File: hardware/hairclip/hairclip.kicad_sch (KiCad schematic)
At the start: 18 parts, among them J1 Conn_Coaxial_Small, J2 Conn_ARM_SWD_TagConnect_TC2030, U1 NRF52840-CKAA-R, U2 MIC5365-3.3YD5, X1 32MHz, X2 32kHz768

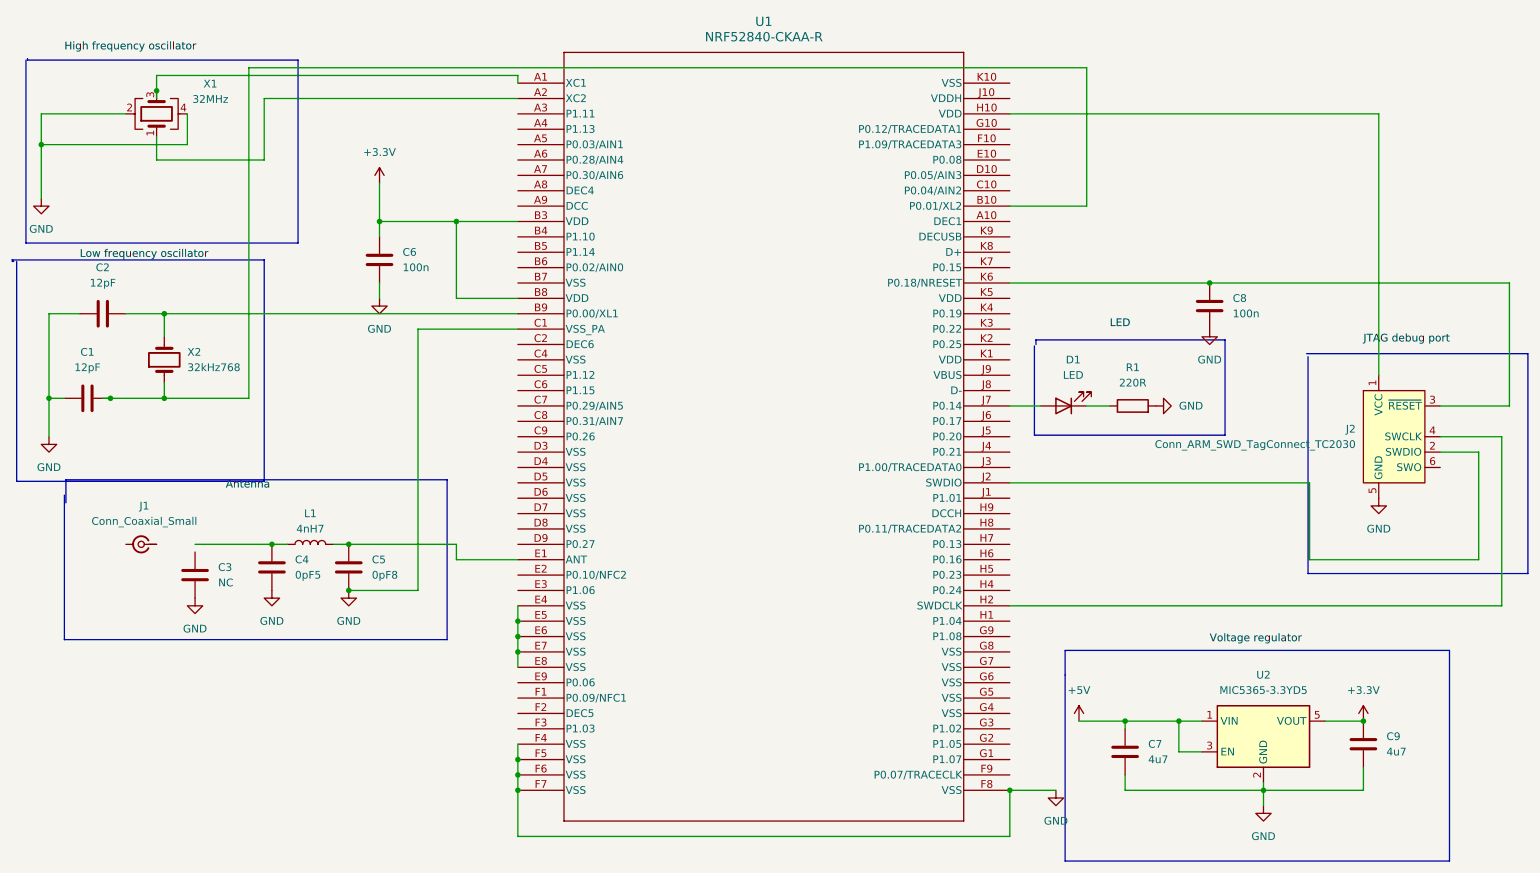
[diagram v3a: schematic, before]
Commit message: add readme images
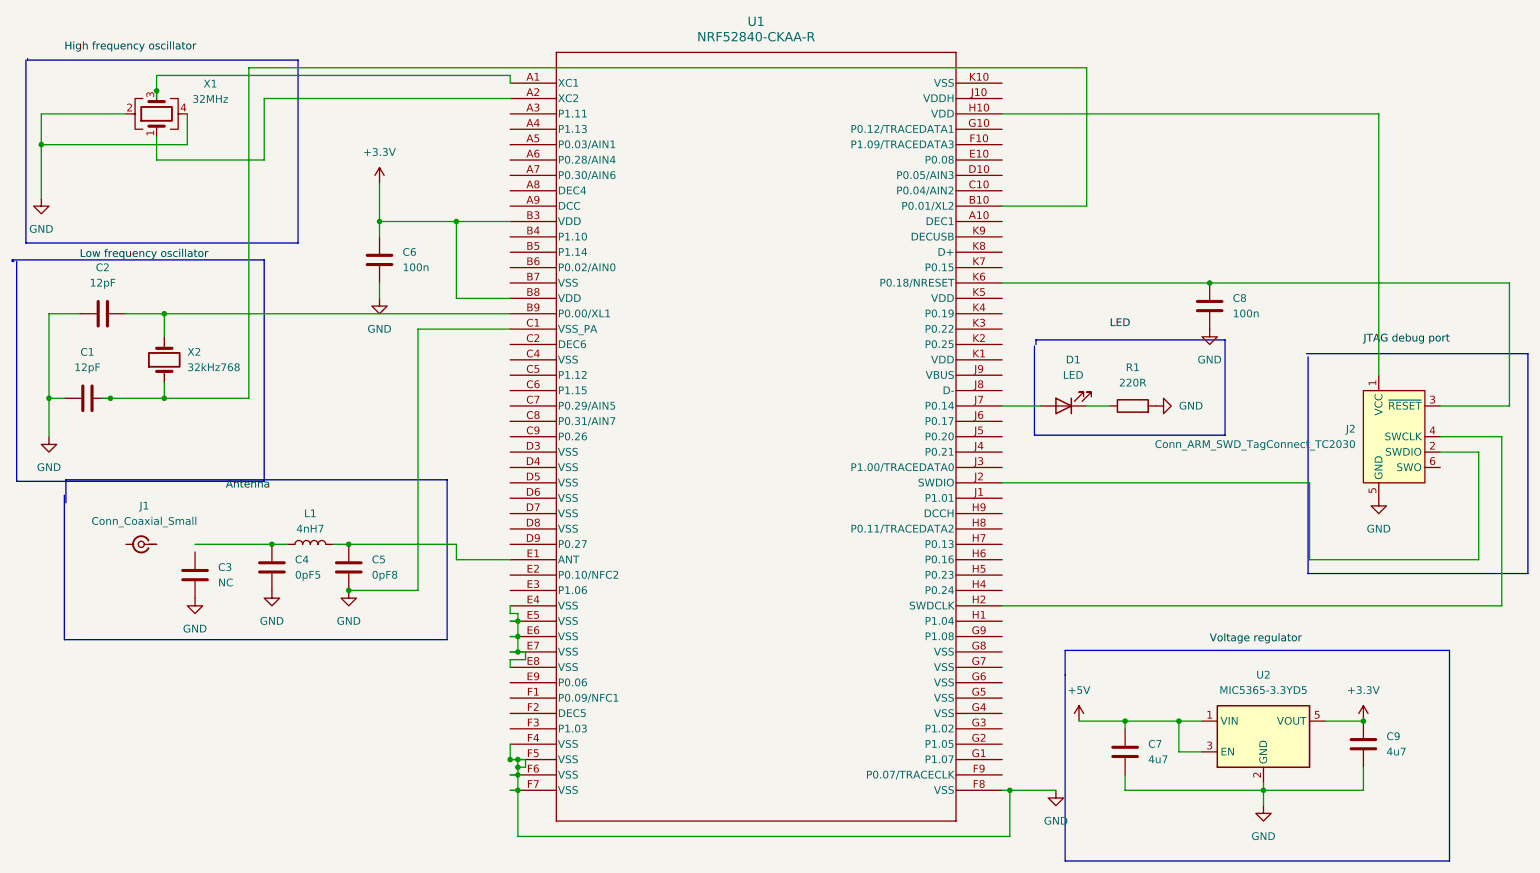
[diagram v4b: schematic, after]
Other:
- moved on the sheet: U1
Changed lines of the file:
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@@
+	)
+	(junction
+		(at 180.34 158.75)
+		(diameter 0)
+		(color 0 0 0 0)
+	)
+	(junction
+		(at 99.06 135.89)
+		(diameter 0)
+		(color 0 0 0 0)
 	)
 	(junction
@@
 	)
 	(junction
+		(at 99.06 153.67)
+		(diameter 0)
+		(color 0 0 0 0)
+	)
+	(junction
 		(at 213.36 74.93)
 		(diameter 0)
@@
 	)
 	(junction
+		(at 99.06 154.94)
+		(diameter 0)
+		(color 0 0 0 0)
+	)
+	(junction
 		(at 99.06 158.75)
 		(diameter 0)
@@
 	)
 	(junction
+		(at 97.79 153.67)
+		(diameter 0)
+		(color 0 0 0 0)
+	)
+	(junction
 		(at 58.42 118.11)
 		(diameter 0)
@@
 	)
 	(junction
-		(at 99.06 135.89)
-		(diameter 0)
-		(color 0 0 0 0)
-	)
-	(junction
-		(at 99.06 153.67)
-		(diameter 0)
-		(color 0 0 0 0)
-	)
-	(junction
-		(at 180.34 158.75)
-		(diameter 0)
-		(color 0 0 0 0)
-	)
-	(junction
 		(at 71.12 118.11)
 		(diameter 0)
@@
 	(wire
 		(pts
+			(xy 97.79 130.81) (xy 99.06 130.81)
+		)
+		(stroke
+			(width 0)
+			(type default)
+		)
+	)
+	(wire
+		(pts
 			(xy 262.89 95.25) (xy 251.46 95.25)
 		)
@@
 		)
 	)
+	(wire
+		(pts
+			(xy 179.07 158.75) (xy 180.34 158.75)
+		)
+		(stroke
+			(width 0)
+			(type default)
+		)
+	)
 	(polyline
 		(pts
@@
 	(wire
 		(pts
-			(xy 180.34 74.93) (xy 213.36 74.93)
+			(xy 179.07 74.93) (xy 213.36 74.93)
 		)
 		(stroke
@@
 	(wire
 		(pts
-			(xy 180.34 128.27) (xy 261.62 128.27)
-		)
-		(stroke
-			(width 0)
-			(type default)
-		)
-	)
-	(wire
-		(pts
-			(xy 180.34 95.25) (xy 185.42 95.25)
+			(xy 179.07 128.27) (xy 261.62 128.27)
+		)
+		(stroke
+			(width 0)
+			(type default)
+		)
+	)
+	(wire
+		(pts
+			(xy 179.07 95.25) (xy 185.42 95.25)
 		)
 		(stroke
@@
 	(wire
 		(pts
-			(xy 40.64 80.01) (xy 99.06 80.01)
+			(xy 100.33 137.16) (xy 100.33 135.89)
+		)
+		(stroke
+			(width 0)
+			(type default)
+		)
+	)
+	(wire
+		(pts
+			(xy 40.64 80.01) (xy 97.79 80.01)
 		)
 		(stroke
@@
 		)
 	)
+	(wire
+		(pts
+			(xy 97.79 135.89) (xy 99.06 135.89)
+		)
+		(stroke
+			(width 0)
+			(type default)
+		)
+	)
 	(polyline
 		(pts
@@
 	(wire
 		(pts
-			(xy 57.15 44.45) (xy 99.06 44.45)
+			(xy 57.15 44.45) (xy 97.79 44.45)
 		)
 		(stroke
@@
 	(wire
 		(pts
-			(xy 99.06 128.27) (xy 99.06 130.81)
+			(xy 97.79 128.27) (xy 97.79 129.54)
 		)
 		(stroke
@@
 	(wire
 		(pts
-			(xy 99.06 153.67) (xy 99.06 156.21)
+			(xy 99.06 153.67) (xy 99.06 154.94)
 		)
 		(stroke
@@
 	(wire
 		(pts
+			(xy 97.79 133.35) (xy 99.06 133.35)
+		)
+		(stroke
+			(width 0)
+			(type default)
+		)
+	)
+	(wire
+		(pts
 			(xy 88.9 77.47) (xy 88.9 64.77)
 		)
@@
 	(wire
 		(pts
-			(xy 180.34 107.95) (xy 229.87 107.95)
+			(xy 99.06 153.67) (xy 100.33 153.67)
+		)
+		(stroke
+			(width 0)
+			(type default)
+		)
+	)
+	(wire
+		(pts
+			(xy 179.07 107.95) (xy 229.87 107.95)
 		)
 		(stroke
@@
 		)
 	)
+	(wire
+		(pts
+			(xy 97.79 158.75) (xy 99.06 158.75)
+		)
+		(stroke
+			(width 0)
+			(type default)
+		)
+	)
+	(wire
+		(pts
+			(xy 97.79 153.67) (xy 99.06 153.67)
+		)
+		(stroke
+			(width 0)
+			(type default)
+		)
+	)
 	(polyline
 		(pts
@@
 	(wire
 		(pts
+			(xy 99.06 135.89) (xy 100.33 135.89)
+		)
+		(stroke
+			(width 0)
+			(type default)
+		)
+	)
+	(wire
+		(pts
 			(xy 199.39 158.75) (xy 222.25 158.75)
 		)
@@
 	(wire
 		(pts
-			(xy 180.34 62.23) (xy 193.04 62.23)
+			(xy 179.07 62.23) (xy 193.04 62.23)
 		)
 		(stroke
@@
 	(wire
 		(pts
-			(xy 99.06 120.65) (xy 88.9 120.65)
-		)
-		(stroke
-			(width 0)
-			(type default)
-		)
-	)
-	(wire
-		(pts
-			(xy 99.06 40.64) (xy 99.06 41.91)
+			(xy 97.79 120.65) (xy 88.9 120.65)
+		)
+		(stroke
+			(width 0)
+			(type default)
+		)
+	)
+	(wire
+		(pts
+			(xy 97.79 40.64) (xy 97.79 41.91)
 		)
 		(stroke
@@
 	(wire
 		(pts
-			(xy 99.06 82.55) (xy 82.55 82.55)
+			(xy 97.79 82.55) (xy 82.55 82.55)
 		)
 		(stroke
@@
 	(wire
 		(pts
+			(xy 97.79 129.54) (xy 99.06 129.54)
+		)
+		(stroke
+			(width 0)
+			(type default)
+		)
+	)
+	(wire
+		(pts
 			(xy 54.61 39.37) (xy 54.61 93.98)
 		)
@@
 	(wire
 		(pts
+			(xy 99.06 129.54) (xy 99.06 130.81)
+		)
+		(stroke
+			(width 0)
+			(type default)
+		)
+	)
+	(wire
+		(pts
 			(xy 238.76 158.75) (xy 222.25 158.75)
 		)
@@
 	(wire
 		(pts
-			(xy 39.37 40.64) (xy 99.06 40.64)
-		)
-		(stroke
-			(width 0)
-			(type default)
-		)
-	)
-	(wire
-		(pts
-			(xy 88.9 64.77) (xy 99.06 64.77)
+			(xy 39.37 40.64) (xy 97.79 40.64)
+		)
+		(stroke
+			(width 0)
+			(type default)
+		)
+	)
+	(wire
+		(pts
+			(xy 88.9 64.77) (xy 97.79 64.77)
+		)
+		(stroke
+			(width 0)
+			(type default)
+		)
+	)
+	(wire
+		(pts
+			(xy 97.79 137.16) (xy 100.33 137.16)
 		)
 		(stroke
@@
 	(wire
 		(pts
+			(xy 99.06 154.94) (xy 99.06 156.21)
+		)
+		(stroke
+			(width 0)
+			(type default)
+		)
+	)
+	(wire
+		(pts
 			(xy 251.46 100.33) (xy 261.62 100.33)
 		)
@@
 	(wire
 		(pts
-			(xy 99.06 77.47) (xy 88.9 77.47)
-		)
-		(stroke
-			(width 0)
-			(type default)
-		)
-	)
-	(wire
-		(pts
-			(xy 99.06 135.89) (xy 99.06 138.43)
+			(xy 97.79 77.47) (xy 88.9 77.47)
+		)
+		(stroke
+			(width 0)
+			(type default)
+		)
+	)
+	(wire
+		(pts
+			(xy 97.79 137.16) (xy 97.79 138.43)
 		)
 		(stroke
@@
 	(wire
 		(pts
-			(xy 99.06 151.13) (xy 99.06 153.67)
+			(xy 100.33 154.94) (xy 99.06 154.94)
+		)
+		(stroke
+			(width 0)
+			(type default)
+		)
+	)
+	(wire
+		(pts
+			(xy 100.33 153.67) (xy 100.33 154.94)
+		)
+		(stroke
+			(width 0)
+			(type default)
+		)
+	)
+	(wire
+		(pts
+			(xy 97.79 151.13) (xy 97.79 153.67)
 		)
 		(stroke
@@
 	(wire
 		(pts
-			(xy 180.34 46.99) (xy 241.3 46.99)
+			(xy 179.07 46.99) (xy 241.3 46.99)
+		)
+		(stroke
+			(width 0)
+			(type default)
+		)
+	)
+	(wire
+		(pts
+			(xy 97.79 156.21) (xy 99.06 156.21)
 		)
 		(stroke
@@
 	(symbol
 		(lib_id "NRF52840-CKAA-R:NRF52840-CKAA-R")
-		(at 99.06 41.91 0)
+		(at 97.79 41.91 0)
 		(unit 1)
 		(exclude_from_sim no)
@@
 		(fields_autoplaced yes)
 		(property "Reference" "U1"
-			(at 139.7 31.75 0)
+			(at 138.43 31.75 0)
 			(effects
 				(font
@@
 		)
 		(property "Value" "NRF52840-CKAA-R"
-			(at 139.7 34.29 0)
+			(at 138.43 34.29 0)
 			(effects
 				(font
@@
 		)
 		(property "Footprint" "Package_DFN_QFN:Nordic_AQFN-73-1EP_7x7mm_P0.5mm"
-			(at 99.06 41.91 0)
+			(at 97.79 41.91 0)
 			(effects
 				(font
@@
 		)
 		(property "Datasheet" "NRF52840-CKAA-R"
-			(at 99.06 41.91 0)
+			(at 97.79 41.91 0)
 			(effects
 				(font
@@
 		)
 		(property "Description" ""
-			(at 99.06 41.91 0)
-			(effects
-				(font
+			(at 97.79 41.91 0)
+			(effects
+				(font
